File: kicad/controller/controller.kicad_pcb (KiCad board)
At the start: 2 copper layers, 10 parts, among them J1 Conn_01x07_Male, U1 BluePill_STM32F103C

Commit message: work on kicad
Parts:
- added C3: C, Capacitor_SMD:C_0805_2012Metric, F.Cu at (81.3, 71.1)
- added C4: C, Capacitor_SMD:C_0805_2012Metric, F.Cu at (186.5, 90.2)
- added C5: C, Capacitor_SMD:C_0805_2012Metric, F.Cu at (186.5, 92.7)
- added C6: C, Capacitor_SMD:C_0805_2012Metric, F.Cu at (54.5, 38.7)
- added C7: C, Capacitor_SMD:C_0805_2012Metric, F.Cu at (54.5, 43.8)
- added C8: C, Capacitor_SMD:C_0805_2012Metric, F.Cu at (68.7, 90.0)
- added C9: C, Capacitor_SMD:C_0805_2012Metric, F.Cu at (68.7, 92.5)
- added J2: Conn_01x07_Male, Connector_PinHeader_2.54mm:PinHeader_1x07_P2.54mm_Vertical, B.Cu at (180.3, 81.3)
- added J3: Conn_01x07_Male, Connector_PinHeader_2.54mm:PinHeader_1x07_P2.54mm_Vertical, B.Cu at (59.8, 32.4)
- added J4: Conn_01x07_Male, Connector_PinHeader_2.54mm:PinHeader_1x07_P2.54mm_Vertical, B.Cu at (75.0, 81.1)
- added J_Boost1: Conn_01x03_Male, Connector_PinHeader_2.54mm:PinHeader_1x03_P2.54mm_Vertical, B.Cu at (154.9, 40.6)
- added J_Button1: Conn_01x05_Male, Connector_PinHeader_2.54mm:PinHeader_1x05_P2.54mm_Vertical, B.Cu at (175.3, 67.3)
- added J_Display1: Conn_01x04_Male, Connector_PinHeader_2.54mm:PinHeader_1x04_P2.54mm_Vertical, B.Cu at (161.3, 61.0)
- added J_SD1: Conn_01x04_Male, Connector_PinHeader_2.54mm:PinHeader_1x04_P2.54mm_Vertical, B.Cu at (105.4, 52.6)
- added R10: 10k, Resistor_SMD:R_1206_3216Metric, F.Cu at (70.1, 39.4)
- added R11: 10k, Resistor_SMD:R_1206_3216Metric, F.Cu at (69.9, 47.0)
- added R12: 10k, Resistor_SMD:R_1206_3216Metric, F.Cu at (81.4, 91.2)
- added R13: 10k, Resistor_SMD:R_1206_3216Metric, F.Cu at (81.4, 96.3)
- added R14: 10k, Resistor_SMD:R_1206_3216Metric, F.Cu at (168.7, 88.9)
- added R15: 10k, Resistor_SMD:R_1206_3216Metric, F.Cu at (170.0, 100.3)
- added R16: 10k, Resistor_SMD:R_1206_3216Metric, F.Cu at (65.7, 35.6)
- added R17: 10k, Resistor_SMD:R_1206_3216Metric, F.Cu at (70.1, 51.4)
- added R18: 10k, Resistor_SMD:R_1206_3216Metric, F.Cu at (86.5, 88.7)
- added R19: 10k, Resistor_SMD:R_1206_3216Metric, F.Cu at (86.5, 100.1)
- added R20: 10k, Resistor_SMD:R_1206_3216Metric, F.Cu at (173.8, 88.9)
- added R21: 10k, Resistor_SMD:R_1206_3216Metric, F.Cu at (173.8, 94.0)
- added R22: 10k, Resistor_SMD:R_1206_3216Metric, F.Cu at (64.4, 40.0)
- added R23: 10k, Resistor_SMD:R_1206_3216Metric, F.Cu at (64.4, 45.1)
- added R24: 10k, Resistor_SMD:R_1206_3216Metric, F.Cu at (81.4, 88.7)
- added R25: 10k, Resistor_SMD:R_1206_3216Metric, F.Cu at (81.4, 93.8)
- added R26: 10k, Resistor_SMD:R_1206_3216Metric, F.Cu at (190.6, 47.2)
- added R27: 10k, Resistor_SMD:R_1206_3216Metric, F.Cu at (190.6, 55.4)
- added R28: 10k, Resistor_SMD:R_1206_3216Metric, F.Cu at (186.3, 87.6)
- added R29: 10k, Resistor_SMD:R_1206_3216Metric, F.Cu at (186.5, 96.5)
- added R30: 10k, Resistor_SMD:R_1206_3216Metric, F.Cu at (54.0, 41.3)
- added R31: 10k, Resistor_SMD:R_1206_3216Metric, F.Cu at (54.0, 47.0)
- added R32: 10k, Resistor_SMD:R_1206_3216Metric, F.Cu at (68.7, 87.2)
- added R33: 10k, Resistor_SMD:R_1206_3216Metric, F.Cu at (68.7, 96.3)
- added R7: 10k, Resistor_SMD:R_1206_3216Metric, F.Cu at (85.1, 73.7)
- added R8: 10k, Resistor_SMD:R_1206_3216Metric, F.Cu at (173.8, 91.4)
- added R9: 10k, Resistor_SMD:R_1206_3216Metric, F.Cu at (173.8, 96.5)
- added U2: LM324, Package_SO:SOIC-14_3.9x8.7mm_P1.27mm, F.Cu at (72.4, 71.1)
- J1, U1: moved to B.Cu
- moved U1 40.4 mm to (129.5, 67.3), turned to -90 degrees
- moved R2 30.6 mm to (178.9, 55.9)
- moved R3 30.6 mm to (172.3, 48.3), turned to 90 degrees
- moved C2 30.3 mm to (190.1, 52.3)
- moved R6 29.3 mm to (178.9, 53.3)
- moved J1 29.3 mm to (185.0, 40.6), turned to 180 degrees
- moved R1 28.0 mm to (178.9, 50.8)
- moved C1 27.7 mm to (190.1, 49.8)
- moved R5 27.4 mm to (178.9, 48.3)
- moved R4 26.1 mm to (172.3, 58.4), turned to -90 degrees
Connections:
- J1 pad 2: ref -> ref1
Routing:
- net GND: track 19.7 -> 556.4 mm, vias 0 -> 2
- net ref1: track 0.00 -> 236.0 mm
- net +12V: track 0.00 -> 222.7 mm, vias 0 -> 4
- net ref2: track 0.00 -> 196.2 mm
- net +3.3V: track 0.00 -> 182.4 mm, vias 0 -> 2
- net A5: track 0.00 -> 112.7 mm, vias 0 -> 2
- net PWM3: track 0.00 -> 89.9 mm, vias 0 -> 2
- net PWM8: track 0.00 -> 84.0 mm, vias 0 -> 2
- net A6: track 0.00 -> 81.9 mm, vias 0 -> 2
- net PWM7: track 0.00 -> 74.8 mm, vias 0 -> 2
- net PWM6: track 0.00 -> 74.7 mm
- net PWM5: track 0.00 -> 71.7 mm
- net A8: track 0.00 -> 68.5 mm
- net PWM4: track 0.00 -> 67.6 mm, vias 0 -> 2
- net ref3: track 0.00 -> 57.5 mm
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
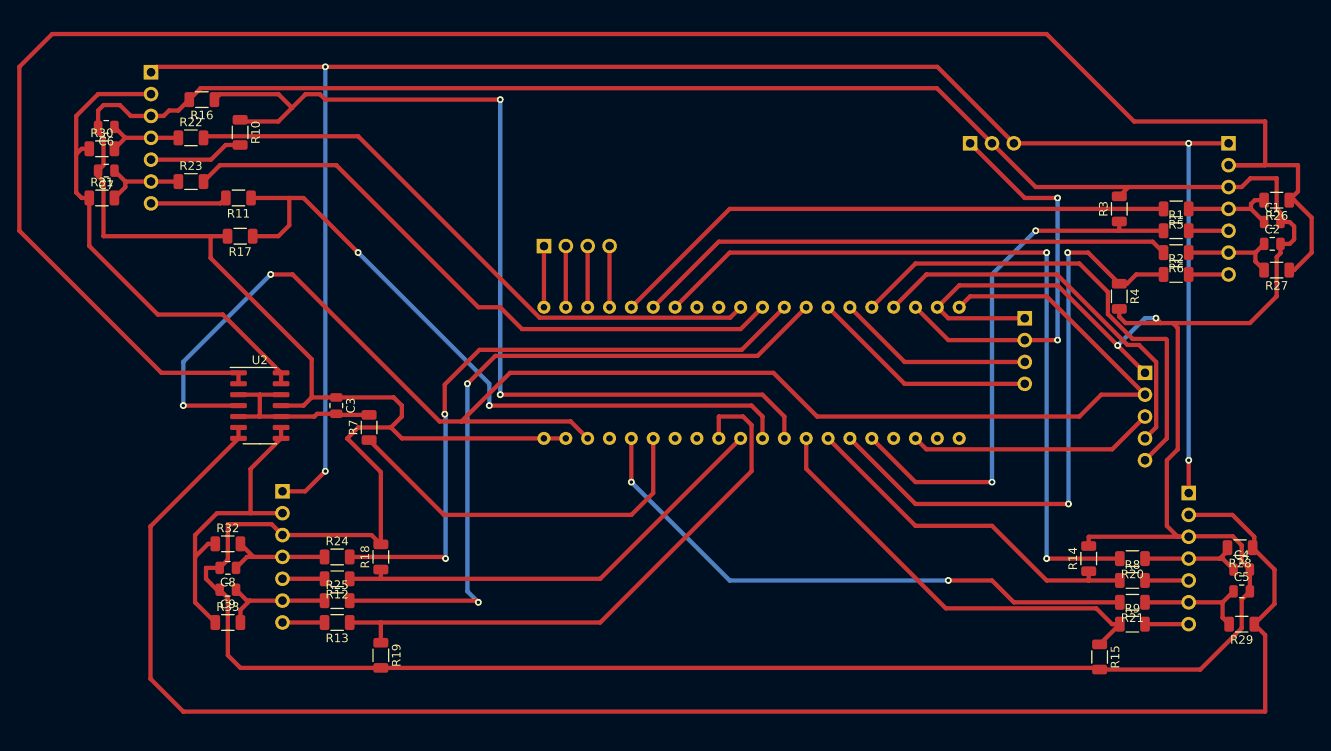
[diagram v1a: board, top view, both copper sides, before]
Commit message: rework PINS, get SD Card working
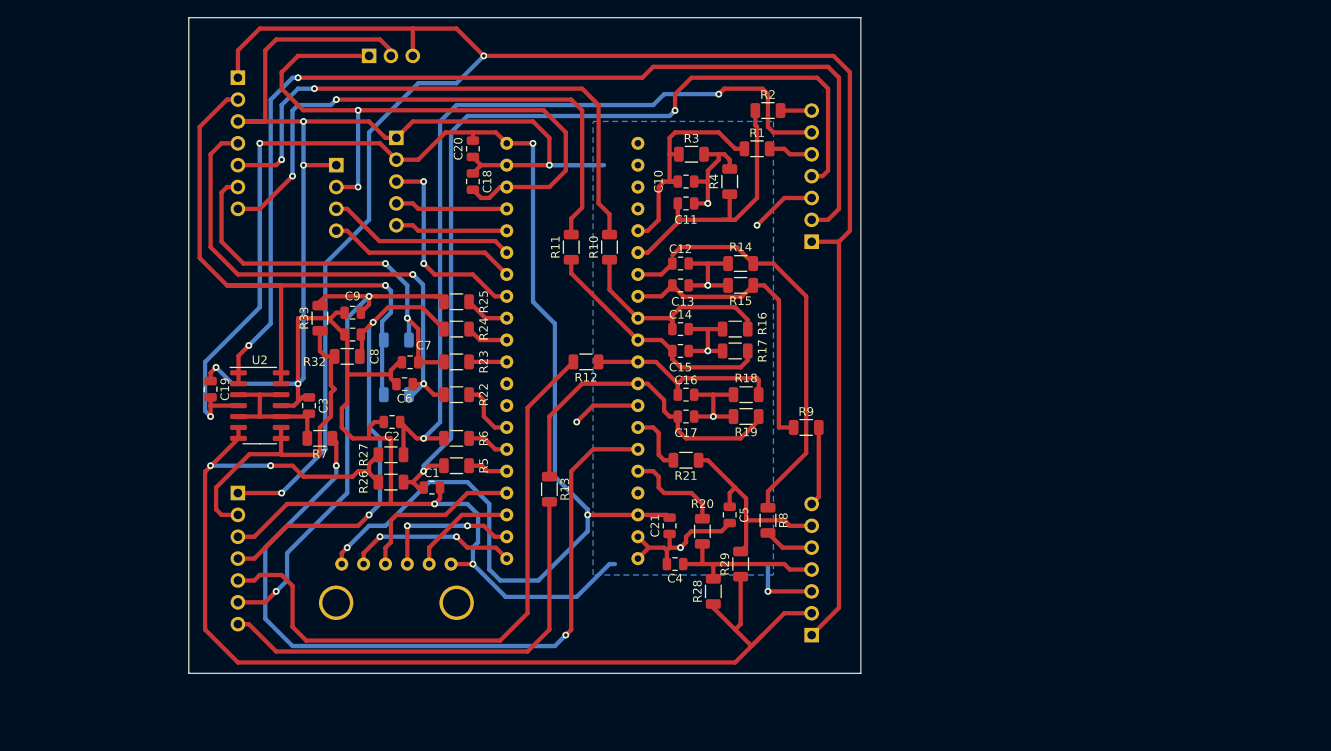
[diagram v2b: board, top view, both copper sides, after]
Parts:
- added C10: C, Capacitor_SMD:C_0805_2012Metric, F.Cu at (121.9, 45.1)
- added C11: C, Capacitor_SMD:C_0805_2012Metric, F.Cu at (121.9, 47.6)
- added C12: C, Capacitor_SMD:C_0805_2012Metric, F.Cu at (121.3, 54.6)
- added C13: C, Capacitor_SMD:C_0805_2012Metric, F.Cu at (121.3, 57.1)
- added C14: C, Capacitor_SMD:C_0805_2012Metric, F.Cu at (121.3, 62.2)
- added C15: C, Capacitor_SMD:C_0805_2012Metric, F.Cu at (121.3, 64.8)
- added C16: C, Capacitor_SMD:C_0805_2012Metric, F.Cu at (121.9, 69.8)
- added C17: C, Capacitor_SMD:C_0805_2012Metric, F.Cu at (121.9, 72.4)
- added C18: C, Capacitor_SMD:C_0805_2012Metric, F.Cu at (97.2, 45.1)
- added C19: C, Capacitor_SMD:C_0805_2012Metric, F.Cu at (66.7, 69.2)
- added C20: C, Capacitor_SMD:C_0805_2012Metric, F.Cu at (97.2, 41.3)
- added C21: C, Capacitor_SMD:C_0805_2012Metric, F.Cu at (120.0, 85.1)
- J_SD1: value Conn_01x04_Male -> Conn_01x06_Male; footprint Connector_PinHeader_2.54mm:PinHeader_1x04_P2.54mm_Vertical -> controller:SD_Card_reader
- R30, R31: moved to B.Cu
- moved R26 108.0 mm to (87.6, 80.0), turned to 0 degrees
- moved R27 105.1 mm to (87.6, 76.8), turned to 0 degrees
- moved C2 104.4 mm to (87.8, 73.0), turned to 180 degrees
- moved C1 102.4 mm to (92.4, 80.6)
- moved J_Button1 91.2 mm to (88.3, 40.0)
- moved R5 88.8 mm to (95.2, 78.1), turned to 0 degrees
- moved R6 86.4 mm to (95.2, 74.9), turned to 0 degrees
- moved J_Display1 82.0 mm to (81.3, 43.2)
- moved J_Boost1 70.6 mm to (85.1, 30.5)
- moved R16 67.5 mm to (127.6, 62.2)
- moved C4 65.9 mm to (120.7, 89.5), turned to 180 degrees
- moved R28 61.4 mm to (125.1, 92.7), turned to 90 degrees
- moved C5 60.2 mm to (127.0, 83.8), turned to -90 degrees
- moved R15 60.0 mm to (128.3, 57.1), turned to 180 degrees
- moved R17 59.1 mm to (127.6, 64.8)
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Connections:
- J_SD1 pad 1: Net-(J_SD1-Pad1) -> +3.3V
- R26 pad 1: ref1 -> ref2
- R27 pad 1: ref1 -> ref2
- U1 pad 14: unconnected-(U1-Pad14) -> PWM4
- U1 pad 16: PWM4 -> PWM3
- U1 pad 21: Net-(J_SD1-Pad1) -> Net-(J_SD1-Pad2)
- U1 pad 22: Net-(J_SD1-Pad2) -> Net-(J_SD1-Pad4)
- U1 pad 23: Net-(J_SD1-Pad3) -> Net-(J_SD1-Pad5)
- U1 pad 24: Net-(J_SD1-Pad4) -> Net-(J_SD1-Pad3)
- U1 pad 27: PWM3 -> PWM5
- U1 pad 3: SW -> unconnected-(U1-Pad3)
- U1 pad 30: PWM5 -> PWM6
- U1 pad 31: PWM6 -> PWM7
- U1 pad 32: PWM7 -> PWM8
- U1 pad 33: PWM8 -> SW
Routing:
- net GND: track 556.4 -> 332.1 mm, vias 2 -> 14
- net ref1: track 236.0 -> 121.7 mm, vias 0 -> 2
- net IN1: track 11.7 -> 107.5 mm, vias 0 -> 2
- net A5: track 112.7 -> 24.7 mm, vias 2 -> 0
- net IN2: track 11.6 -> 96.6 mm, vias 0 -> 2
- net PWM8: track 84.0 -> 5.17 mm, vias 2 -> 0
- net PWM3: track 89.9 -> 11.5 mm, vias 2 -> 0
- net PWM6: track 74.7 -> 4.38 mm
- net PWM7: track 74.8 -> 4.91 mm, vias 2 -> 0
- net U7: track 4.89 -> 72.6 mm
- net PWM5: track 71.7 -> 7.07 mm
- net PWM1: track 66.6 -> 4.64 mm
- net PWM4: track 67.6 -> 7.19 mm, vias 2 -> 0
- net ref2: track 196.2 -> 137.7 mm, vias 0 -> 2
- net PWM2: track 63.0 -> 4.91 mm
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- added copper zone on B.Cu, net GND
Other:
- board outline added: 78.1 x 76.2 mm

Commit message: work on kicad
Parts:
- added J_PWR1: Conn_01x02_Male, Connector_PinHeader_2.54mm:PinHeader_1x02_P2.54mm_Vertical, B.Cu at (83.2, 31.1)
- moved J_Boost1 10.8 mm to (95.9, 31.1)
- moved J_Display1 3.17 mm to (84.5, 43.2)
- moved J_Button1 1.27 mm to (89.5, 40.0)
- moved R5 0.90 mm to (94.6, 77.5)
- moved R6 0.90 mm to (94.6, 74.3)
- moved C19 0.90 mm to (67.3, 69.8)
- moved C1 0.63 mm to (92.4, 80.0)
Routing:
- net GND: track 332.1 -> 347.1 mm
- net +5V: track 76.4 -> 89.2 mm
- net +12V: track 219.3 -> 215.9 mm
- net U6: track 65.2 -> 68.2 mm
- net Net-(J_Display1-Pad4): track 21.9 -> 19.1 mm
- net U5: track 65.7 -> 67.8 mm
- net /SDA: track 21.9 -> 19.9 mm
- net IN2: track 96.6 -> 95.0 mm
- net DT: track 13.1 -> 11.8 mm
- net CLK: track 13.1 -> 11.8 mm
- net IN1: track 107.5 -> 106.3 mm
- net IN7: track 55.7 -> 54.6 mm
- net ref1: track 121.7 -> 122.8 mm
- net +3.3V: track 177.6 -> 176.6 mm
- net REF_IN: track 89.4 -> 88.4 mm
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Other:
- board text added: "V1"

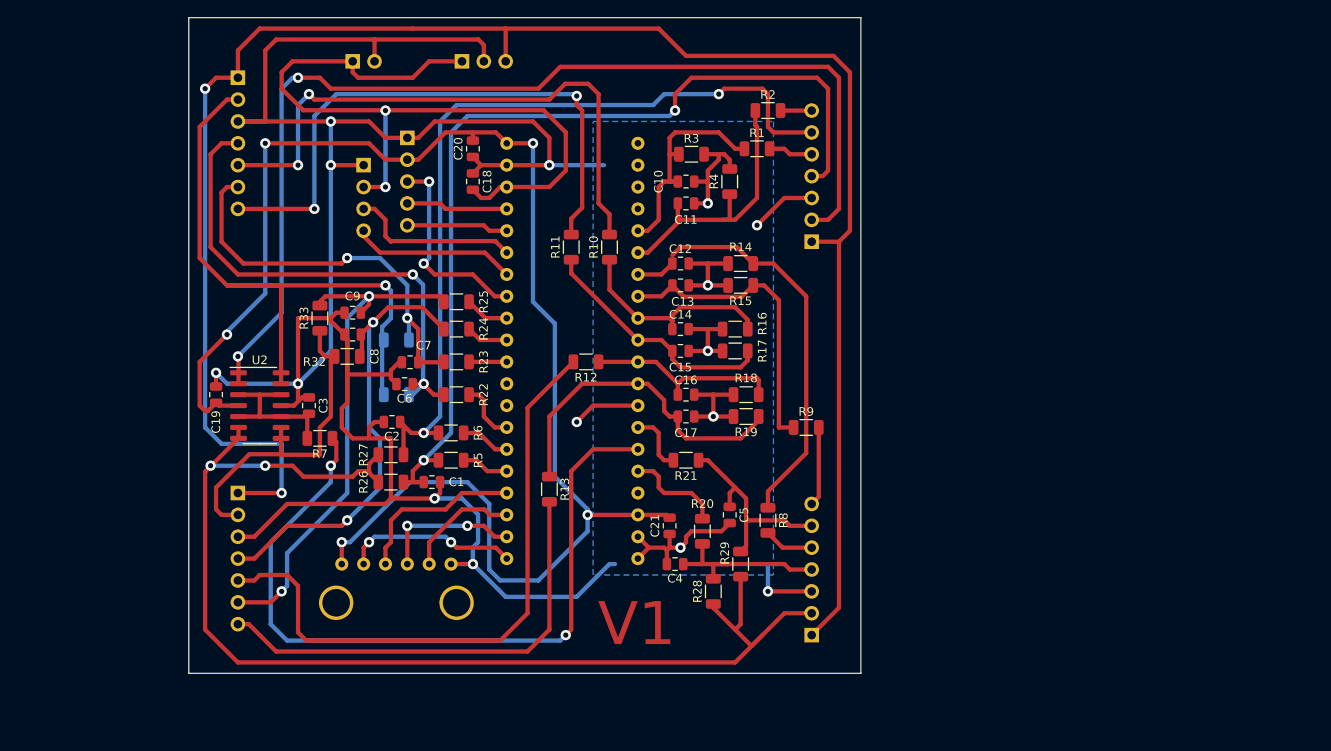
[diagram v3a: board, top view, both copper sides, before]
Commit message: work on pulse charge/discharge, combined board
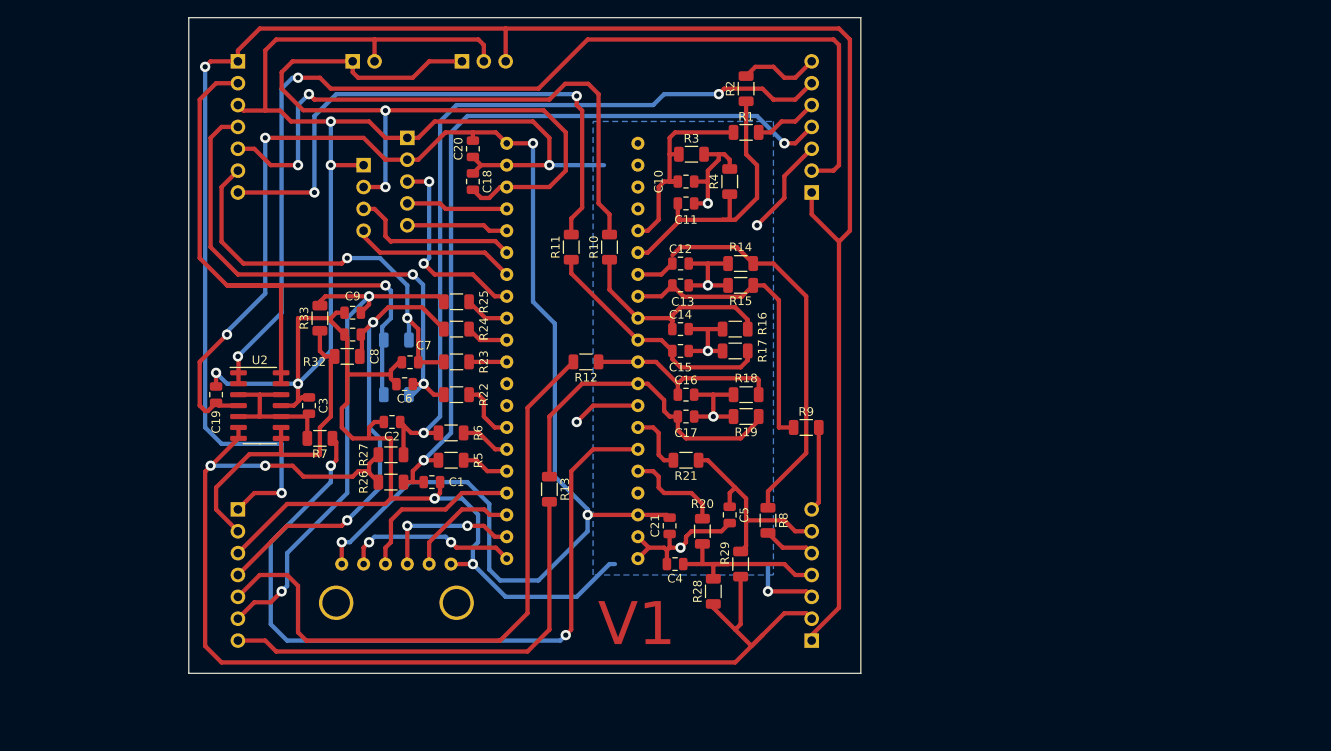
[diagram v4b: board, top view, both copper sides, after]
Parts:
- moved J1 5.72 mm to (136.5, 46.4)
- moved R2 3.59 mm to (128.9, 34.3), turned to 90 degrees
- moved R1 2.29 mm to (128.9, 39.4)
- moved J3 1.91 mm to (69.8, 31.1)
- moved J4 1.91 mm to (69.8, 83.2)
- moved J2 0.63 mm to (136.5, 98.4)
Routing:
- net IN1: track 106.3 -> 91.3 mm
- net +12V: track 215.9 -> 223.7 mm
- net U2: track 3.62 -> 9.38 mm
- net IN2: track 95.0 -> 92.0 mm
- net ref3: track 75.4 -> 78.1 mm
- net U1: track 5.15 -> 7.47 mm
- net A1: track 26.1 -> 24.0 mm
- net U6: track 68.2 -> 66.3 mm
- net IN5: track 58.9 -> 60.8 mm
- net GND: track 347.1 -> 349.0 mm
- net A2: track 32.7 -> 34.3 mm
- net ref2: track 137.7 -> 139.1 mm
- net IN6: track 47.2 -> 48.3 mm
- net +3.3V: track 176.6 -> 177.5 mm
- net U7: track 73.0 -> 73.8 mm
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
